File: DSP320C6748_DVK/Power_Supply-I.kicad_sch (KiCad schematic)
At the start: 32 parts, among them IC4 TPS2087D, IC5 TPS2068DGNR, IC6 SN74AHC1G04DBVR, IC7 TPS3707-33DR, J3 Barrel_Jack_Switch, J4 USB_B_Mini, Q1 MMBT3904LT3G, Q2 MMBT3904LT3G, Q3 MMBT3904LT3G, Q4 MMBT3904LT3G, U2 NCP-347MTAE

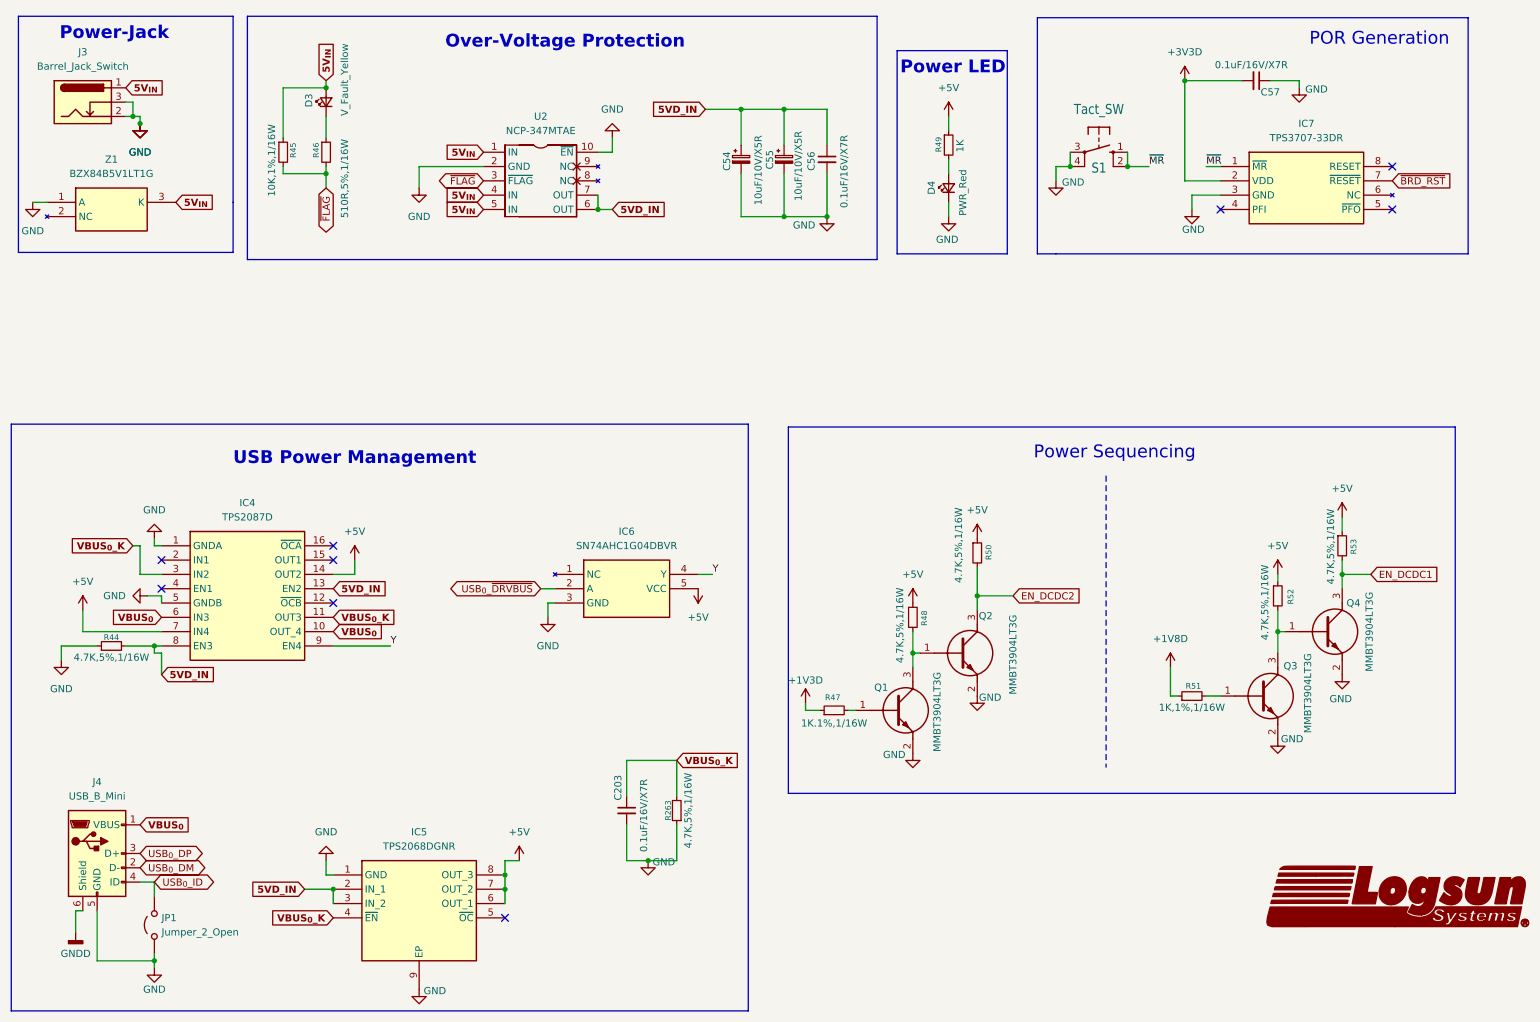
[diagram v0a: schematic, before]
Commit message: DC jack Replaced With Type-C, ADC and RTC section added
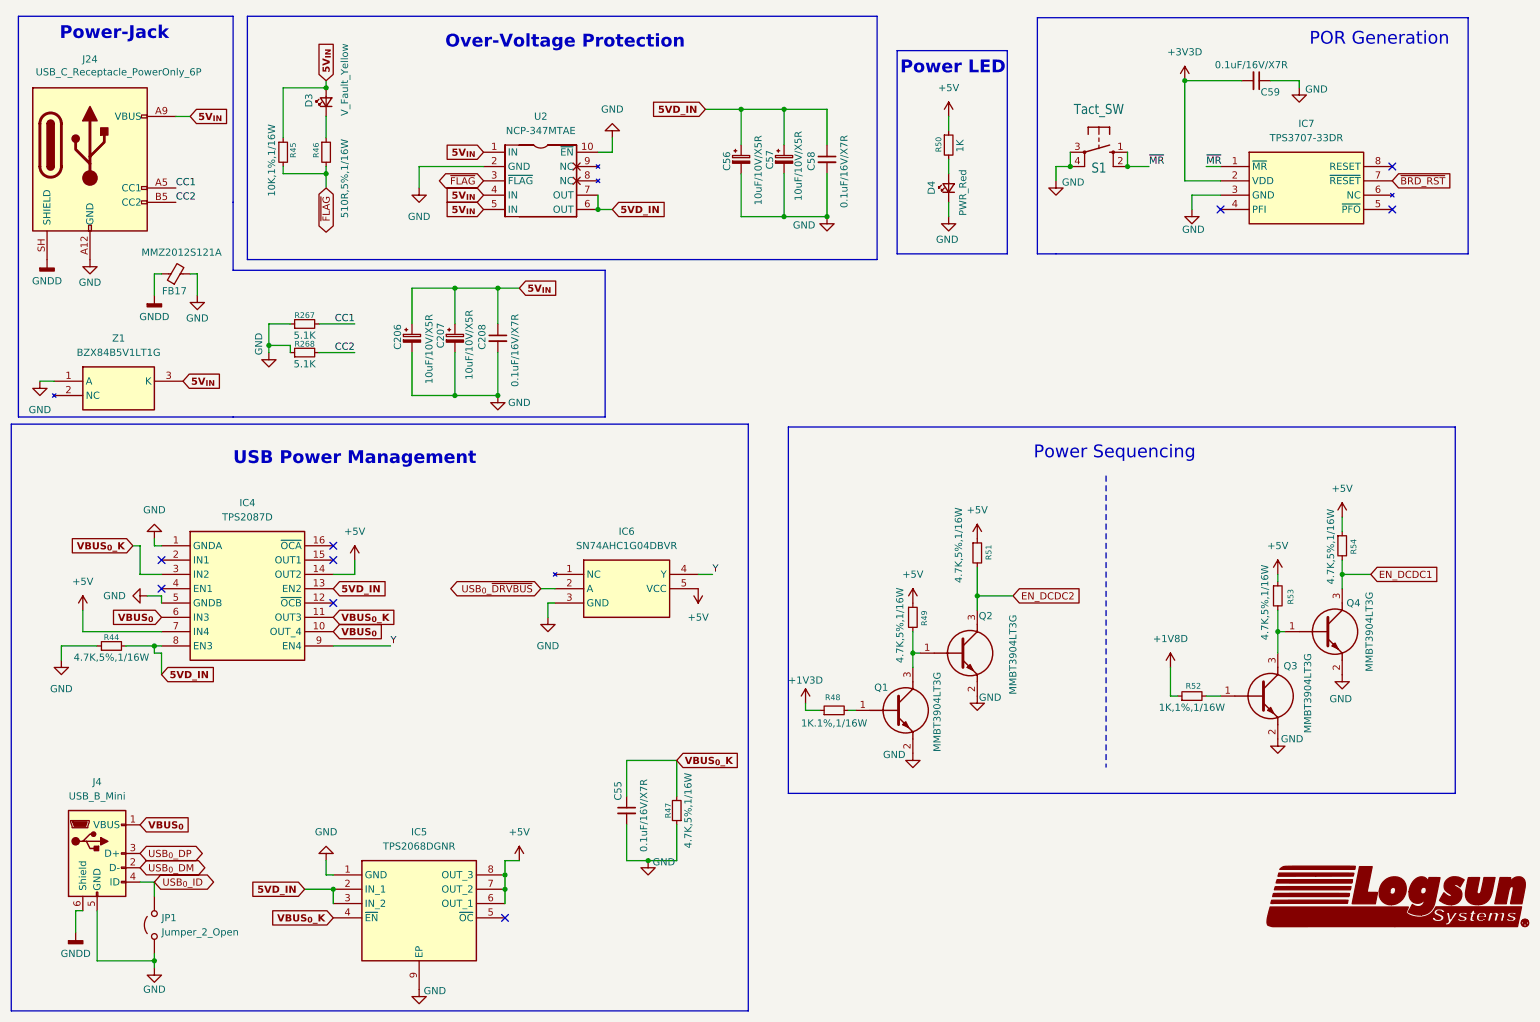
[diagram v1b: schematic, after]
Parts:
- removed J3: Barrel_Jack_Switch, symbol Connector:Barrel_Jack_Switch
- added C206, C207: 10uF/10V/X5R, symbol Device:C_Polarized_Small
- added C208: 0.1uF/16V/X7R, symbol Device:C_Small
- added FB17: MMZ2012S121A, symbol Device:FerriteBead_Small
- added J24: USB_C_Receptacle_PowerOnly_6P, symbol Connector:USB_C_Receptacle_PowerOnly_6P
- added R267, R268: 5.1K, symbol Device:R_Small
- renumbered C203 to C55, C54 to C56, C55 to C57, C56 to C58, C57 to C59, R263 to R47, R47 to R48, R48 to R49, R49 to R50, R50 to R51, R51 to R52, R52 to R53, R53 to R54
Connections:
- net 5V_{IN}: now also C206.1, C207.1, C208.1, J24.A9 (VBUS), J24.B9 (VBUS)
- net GND: now also C206.2, C207.2, C208.2, FB17.2, J24.A12 (GND), J24.B12 (GND), R267.1, R268.1
- net GNDD: now also FB17.1, J24.SH (SHIELD)
- new net CC1: J24.A5 (CC1), R267.2
- new net CC2: J24.B5 (CC2), R268.2
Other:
- moved on the sheet: Z1

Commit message: Scheamtic Re-annotation done, Some footprints assigned
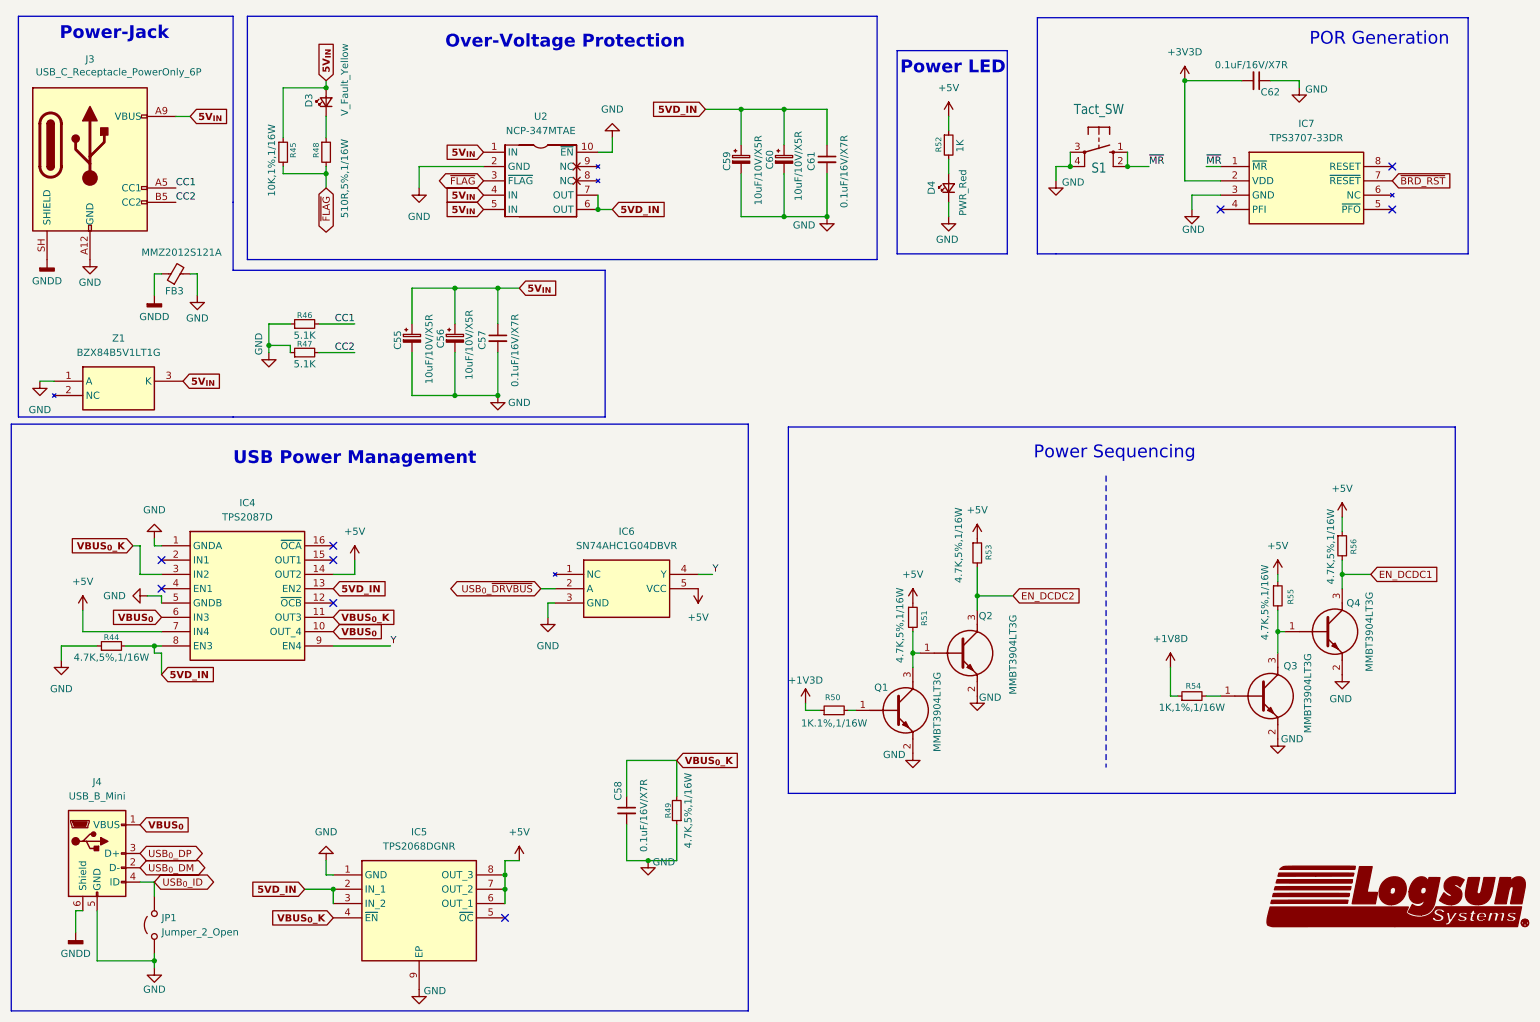
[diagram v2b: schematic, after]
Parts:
- C55: renamed from C206; footprint (none) -> Capacitor_SMD:C_0603_1608Metric_Pad1.08x0.95mm_HandSolder
- C56: renamed from C207; footprint (none) -> Capacitor_SMD:C_0603_1608Metric_Pad1.08x0.95mm_HandSolder
- C57: renamed from C208; footprint (none) -> Capacitor_SMD:C_0603_1608Metric_Pad1.08x0.95mm_HandSolder
- C58: renamed from C55; footprint (none) -> Capacitor_SMD:C_0603_1608Metric_Pad1.08x0.95mm_HandSolder
- C59: renamed from C56; footprint (none) -> Capacitor_SMD:C_0603_1608Metric_Pad1.08x0.95mm_HandSolder
- C60: renamed from C57; footprint (none) -> Capacitor_SMD:C_0603_1608Metric_Pad1.08x0.95mm_HandSolder
- C61: renamed from C58; footprint (none) -> Capacitor_SMD:C_0603_1608Metric_Pad1.08x0.95mm_HandSolder
- C62: renamed from C59; footprint (none) -> Capacitor_SMD:C_0603_1608Metric_Pad1.08x0.95mm_HandSolder
- FB3: renamed from FB17; footprint (none) -> Inductor_SMD:L_0805_2012Metric_Pad1.05x1.20mm_HandSolder
- R44, R45: footprint (none) -> Resistor_SMD:R_0603_1608Metric_Pad0.98x0.95mm_HandSolder
- R46: renamed from R267; footprint (none) -> Resistor_SMD:R_0603_1608Metric_Pad0.98x0.95mm_HandSolder
- R47: renamed from R268; footprint (none) -> Resistor_SMD:R_0603_1608Metric_Pad0.98x0.95mm_HandSolder
- R48: renamed from R46; footprint (none) -> Resistor_SMD:R_0603_1608Metric_Pad0.98x0.95mm_HandSolder
- R49: renamed from R47; footprint (none) -> Resistor_SMD:R_0603_1608Metric_Pad0.98x0.95mm_HandSolder
- R50: renamed from R48; footprint (none) -> Resistor_SMD:R_0603_1608Metric_Pad0.98x0.95mm_HandSolder
- R51: renamed from R49; footprint (none) -> Resistor_SMD:R_0603_1608Metric_Pad0.98x0.95mm_HandSolder
- R52: renamed from R50; footprint (none) -> Resistor_SMD:R_0603_1608Metric_Pad0.98x0.95mm_HandSolder
- R53: renamed from R51; footprint (none) -> Resistor_SMD:R_0603_1608Metric_Pad0.98x0.95mm_HandSolder
- R54: renamed from R52; footprint (none) -> Resistor_SMD:R_0603_1608Metric_Pad0.98x0.95mm_HandSolder
- R55: renamed from R53; footprint (none) -> Resistor_SMD:R_0603_1608Metric_Pad0.98x0.95mm_HandSolder
- R56: renamed from R54; footprint (none) -> Resistor_SMD:R_0603_1608Metric_Pad0.98x0.95mm_HandSolder
- renumbered J24 to J3
